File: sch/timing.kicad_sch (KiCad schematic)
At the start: 18 parts

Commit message: Sch: timing - part annotations
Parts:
- C50, C51: value (none) -> 240pF
- D34, D35: value (none) -> 74LS193
- D36: value (none) -> 74LS93
- D37: value (none) -> 7408
- D43: value (none) -> 74123
- D45: value (none) -> 74LS74
- R11, R12: value (none) -> 7k5
- R13, R17, R29: value (none) -> 1k
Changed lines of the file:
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@@
     (in_bom yes) (on_board yes)
     (property "Reference" "D37" (id 0) (at 250.825 158.75 0))
-    (property "Value" "" (id 1) (at 257.175 158.75 0))
+    (property "Value" "7408" (id 1) (at 257.175 158.75 0))
     (property "Footprint" "" (id 2) (at 254.635 153.035 0)
       (effects (font (size 1.27 1.27)) hide)
@@
       (effects (font (size 1.27 1.27)) (justify left))
     )
-    (property "Value" "" (id 1) (at 203.3144 46.355 0)
+    (property "Value" "74LS93" (id 1) (at 203.3144 46.355 0)
       (effects (font (size 1.27 1.27)) (justify left))
     )
@@
     (in_bom yes) (on_board yes)
     (property "Reference" "D43" (id 0) (at 285.115 42.545 0))
-    (property "Value" "" (id 1) (at 292.1 42.545 0))
+    (property "Value" "74123" (id 1) (at 292.1 42.545 0))
     (property "Footprint" "" (id 2) (at 288.925 53.975 0)
       (effects (font (size 1.27 1.27)) hide)
@@
       (effects (font (size 1.27 1.27)) (justify left))
     )
-    (property "Value" "" (id 1) (at 205.105 144.145 0)
+    (property "Value" "74LS74" (id 1) (at 205.105 144.145 0)
       (effects (font (size 1.27 1.27)) (justify left))
     )
@@
       (effects (font (size 1.27 1.27)) (justify left))
     )
-    (property "Value" "" (id 1) (at 78.8544 44.45 0)
+    (property "Value" "74LS193" (id 1) (at 78.8544 44.45 0)
       (effects (font (size 1.27 1.27)) (justify left))
     )
@@
       (effects (font (size 1.27 1.27)) (justify left))
     )
-    (property "Value" "" (id 1) (at 272.415 40.005 90)
+    (property "Value" "7k5" (id 1) (at 272.415 40.005 90)
       (effects (font (size 1.27 1.27)) (justify left))
     )
@@
       (effects (font (size 1.27 1.27)) (justify left))
     )
-    (property "Value" "" (id 1) (at 48.26 31.115 90)
+    (property "Value" "1k" (id 1) (at 48.26 31.115 90)
       (effects (font (size 1.27 1.27)) (justify left))
     )
@@
       (effects (font (size 1.27 1.27)) (justify left))
     )
-    (property "Value" "" (id 1) (at 262.89 136.525 90)
+    (property "Value" "7k5" (id 1) (at 262.89 136.525 90)
       (effects (font (size 1.27 1.27)) (justify left))
     )
@@
     (in_bom yes) (on_board yes)
     (property "Reference" "D43" (id 0) (at 277.495 139.065 0))
-    (property "Value" "" (id 1) (at 284.48 139.065 0))
+    (property "Value" "74123" (id 1) (at 284.48 139.065 0))
     (property "Footprint" "" (id 2) (at 280.035 150.495 0)
       (effects (font (size 1.27 1.27)) hide)
@@
     (in_bom yes) (on_board yes)
     (property "Reference" "R17" (id 0) (at 316.865 61.595 0))
-    (property "Value" "" (id 1) (at 316.865 64.135 0))
+    (property "Value" "1k" (id 1) (at 316.865 64.135 0))
     (property "Footprint" "" (id 2) (at 313.055 62.865 0)
       (effects (font (size 1.27 1.27)) hide)
@@
       (effects (font (size 1.27 1.27)) (justify left))
     )
-    (property "Value" "" (id 1) (at 152.5144 45.085 0)
+    (property "Value" "74LS193" (id 1) (at 152.5144 45.085 0)
       (effects (font (size 1.27 1.27)) (justify left))
     )
@@
       (effects (font (size 1.27 1.27)) (justify right))
     )
-    (property "Value" "" (id 1) (at 253.365 145.415 0)
+    (property "Value" "240pF" (id 1) (at 253.365 145.415 0)
       (effects (font (size 1.27 1.27)) (justify right))
     )
@@
     (in_bom yes) (on_board yes)
     (property "Reference" "R13" (id 0) (at 194.945 144.145 0))
-    (property "Value" "" (id 1) (at 195.58 146.685 0))
+    (property "Value" "1k" (id 1) (at 195.58 146.685 0))
     (property "Footprint" "" (id 2) (at 200.025 145.415 0)
       (effects (font (size 1.27 1.27)) hide)
@@
       (effects (font (size 1.27 1.27)) (justify right))
     )
-    (property "Value" "" (id 1) (at 262.255 48.895 0)
+    (property "Value" "240pF" (id 1) (at 262.255 48.895 0)
       (effects (font (size 1.27 1.27)) (justify right))
     )
@@
     (in_bom yes) (on_board yes)
     (property "Reference" "D37" (id 0) (at 257.81 64.135 0))
-    (property "Value" "" (id 1) (at 264.16 64.135 0))
+    (property "Value" "7408" (id 1) (at 264.16 64.135 0))
     (property "Footprint" "" (id 2) (at 262.255 56.515 0)
       (effects (font (size 1.27 1.27)) hide)

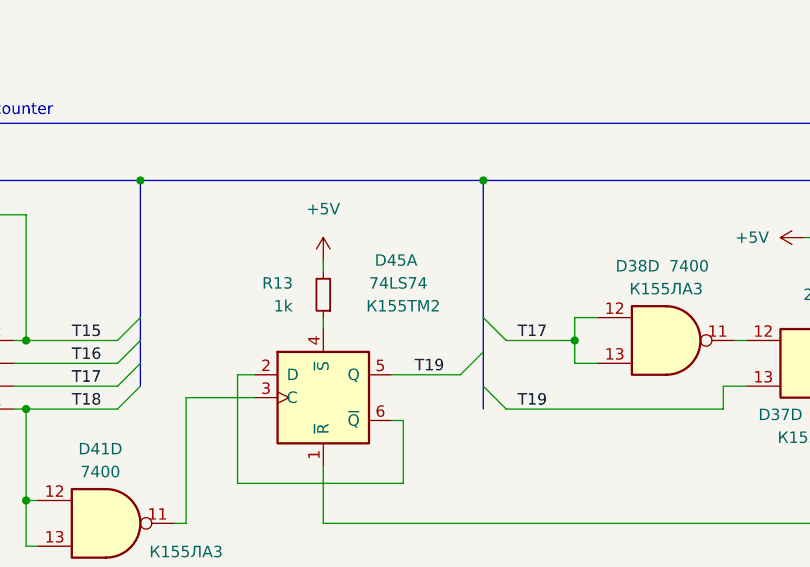
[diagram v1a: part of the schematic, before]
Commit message: Schematics completed with values
Visual corrections pending
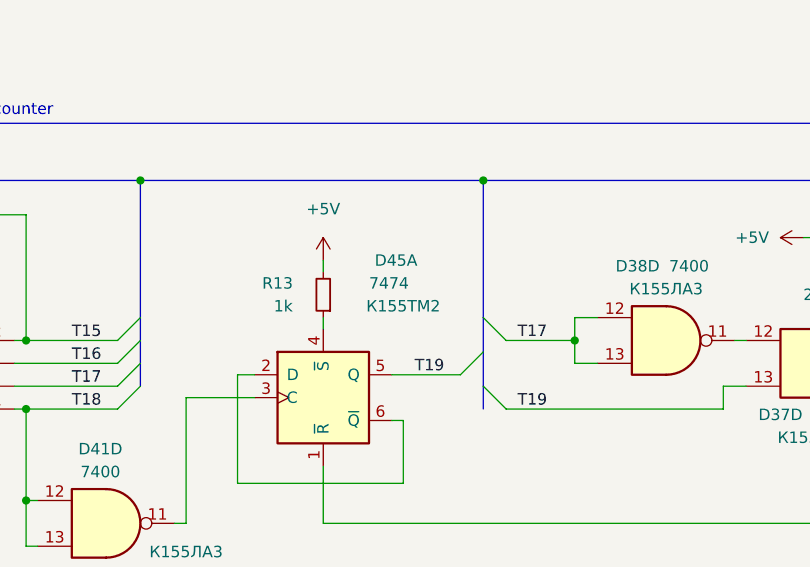
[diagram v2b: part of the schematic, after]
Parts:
- D39, D40: CCCP (none) -> К555ИЕ5
- D45: value 74LS74 -> 7474
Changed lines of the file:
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@@
       (effects (font (size 1.27 1.27)) (justify left))
     )
-    (property "Value" "74LS74" (id 1) (at 205.105 144.145 0)
+    (property "Value" "7474" (id 1) (at 205.105 144.145 0)
       (effects (font (size 1.27 1.27)) (justify left))
     )
@@
       (effects (font (size 1.27 1.27)) hide)
     )
+    (property "CCCP" "К555ИЕ5" (id 4) (at 153.035 155.575 0)
+      (effects (font (size 1.27 1.27)) hide)
+    )
     (pin "1")
     (pin "10")
@@
       (effects (font (size 1.27 1.27)) hide)
     )
+    (property "CCCP" "К555ИЕ5" (id 4) (at 100.965 155.575 0)
+      (effects (font (size 1.27 1.27)) hide)
+    )

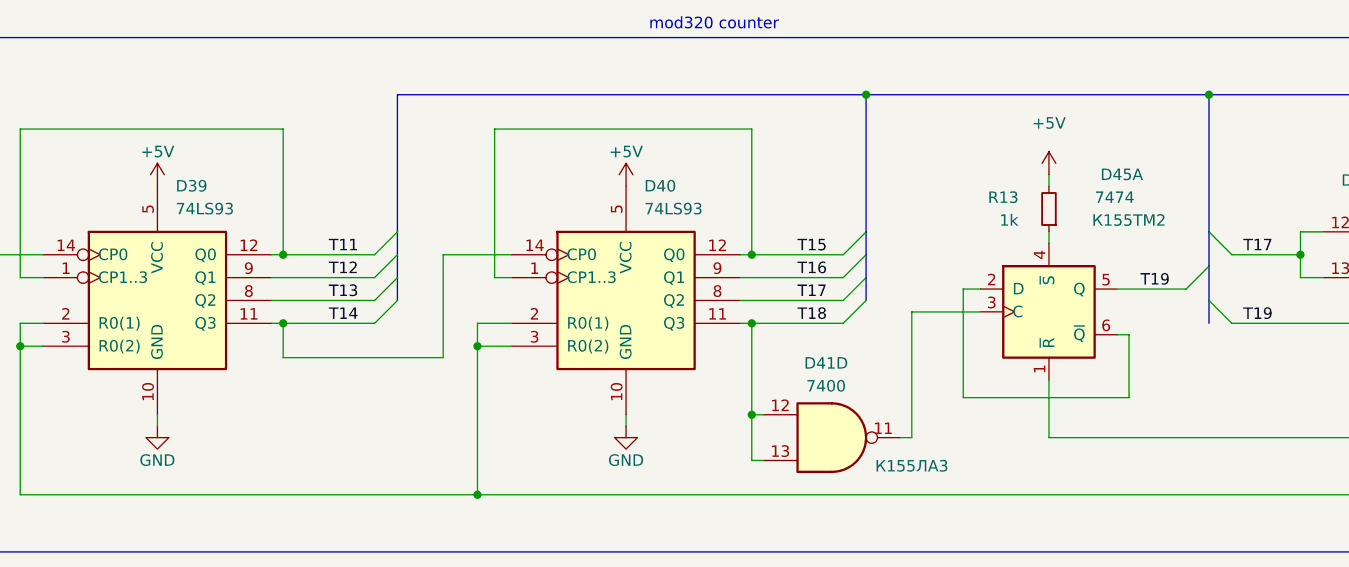
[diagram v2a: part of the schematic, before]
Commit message: Sch: visual corrections
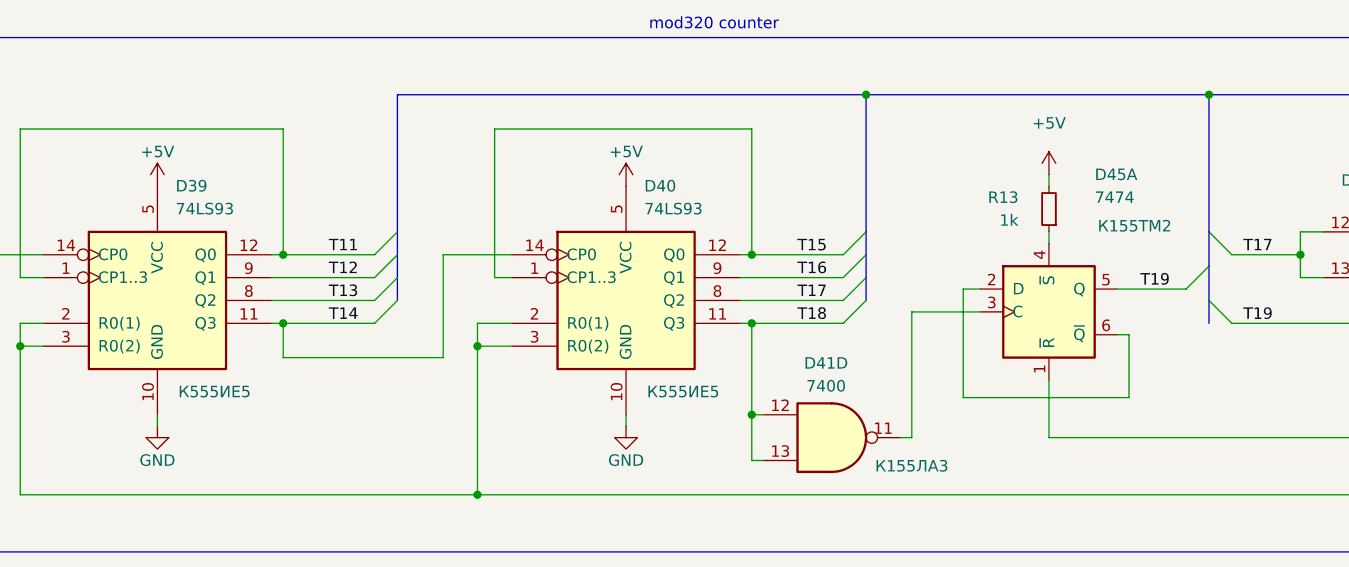
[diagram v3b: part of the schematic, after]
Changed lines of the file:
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@@
   (symbol (lib_id "74xx:74LS74") (at 200.025 156.845 0) (unit 1)
     (in_bom yes) (on_board yes)
-    (property "Reference" "D45" (id 0) (at 205.74 141.605 0)
+    (property "Reference" "D45" (id 0) (at 205.105 141.605 0)
       (effects (font (size 1.27 1.27)) (justify left))
     )
@@
       (effects (font (size 1.27 1.27)) hide)
     )
-    (property "CCCP" "К155ТМ2" (id 4) (at 208.915 146.685 0))
+    (property "CCCP" "К155ТМ2" (id 4) (at 209.55 147.32 0))
     (pin "1")
     (pin "2")
@@
   )
   (symbol (lib_id "74xx:74LS93") (at 153.035 155.575 0) (unit 1)
-    (in_bom yes) (on_board yes) (fields_autoplaced)
+    (in_bom yes) (on_board yes)
     (property "Reference" "D40" (id 0) (at 155.0544 142.875 0)
       (effects (font (size 1.27 1.27)) (justify left))
@@
       (effects (font (size 1.27 1.27)) hide)
     )
-    (property "CCCP" "К555ИЕ5" (id 4) (at 153.035 155.575 0)
-      (effects (font (size 1.27 1.27)) hide)
-    )
+    (property "CCCP" "К555ИЕ5" (id 4) (at 159.385 165.735 0))
     (pin "1")
     (pin "10")
@@
   )
   (symbol (lib_id "74xx:74LS93") (at 100.965 155.575 0) (unit 1)
-    (in_bom yes) (on_board yes) (fields_autoplaced)
+    (in_bom yes) (on_board yes)
     (property "Reference" "D39" (id 0) (at 102.9844 142.875 0)
       (effects (font (size 1.27 1.27)) (justify left))
@@
       (effects (font (size 1.27 1.27)) hide)
     )
-    (property "CCCP" "К555ИЕ5" (id 4) (at 100.965 155.575 0)
-      (effects (font (size 1.27 1.27)) hide)
-    )
-    (pin "1")
-    (pin "10")
+    (property "CCCP" "К555ИЕ5" (id 4) (at 107.315 165.735 0))
+    (pin "1")
+    (pin "10")
